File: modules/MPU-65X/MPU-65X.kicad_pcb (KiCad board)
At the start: 2 copper layers, 160 x 100 mm, 11 parts, among them J1 CardConnector, J2 DE9_Socket, U1 6502, U2 28C256, U3 62256, U4 74NC00, U5 W65C51, U6 W65C22, U8 MAX232, Y1 1Mhz

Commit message: added joshua
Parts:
- added D1: RI, LED_THT:LED_D5.0mm_Horizontal_O1.27mm_Z9.0mm, F.Cu at (65.2, 56.9)
- added D2: DTR, LED_THT:LED_D5.0mm_Horizontal_O1.27mm_Z9.0mm, F.Cu at (65.2, 63.5)
- added D3: DCD, LED_THT:LED_D5.0mm_Horizontal_O1.27mm_Z9.0mm, F.Cu at (65.2, 70.1)
- added D4: DSR, LED_THT:LED_D5.0mm_Horizontal_O1.27mm_Z9.0mm, F.Cu at (65.2, 76.7)
- added D5: RTS, LED_THT:LED_D5.0mm_Horizontal_O1.27mm_Z3.0mm, F.Cu at (62.0, 70.1)
- added D6: RTR, LED_THT:LED_D5.0mm_Horizontal_O1.27mm_Z3.0mm, F.Cu at (62.0, 83.3)
- added D7: CTS, LED_THT:LED_D5.0mm_Horizontal_O1.27mm_Z3.0mm, F.Cu at (62.0, 76.7)
- added D8: T_{X}D, LED_THT:LED_D5.0mm_Horizontal_O1.27mm_Z3.0mm, F.Cu at (62.0, 56.9)
- added D9: R_{X}D, LED_THT:LED_D5.0mm_Horizontal_O1.27mm_Z3.0mm, F.Cu at (62.0, 63.5)
- added R1: 1kΩ, IMNOTWOPR:R_Axial_DIN0207_P400mil, F.Cu at (74.7, 59.4)
- added R2: 1kΩ, IMNOTWOPR:R_Axial_DIN0207_P400mil, F.Cu at (74.7, 63.3)
- added R3: 1kΩ, IMNOTWOPR:R_Axial_DIN0207_P400mil, F.Cu at (74.7, 67.2)
- added R4: 1kΩ, IMNOTWOPR:R_Axial_DIN0207_P400mil, F.Cu at (74.7, 71.0)
- added R5: 1kΩ, IMNOTWOPR:R_Axial_DIN0207_P400mil, F.Cu at (74.7, 74.9)
- added R6: 1kΩ, IMNOTWOPR:R_Axial_DIN0207_P400mil, F.Cu at (74.7, 78.7)
- added R7: 1kΩ, IMNOTWOPR:R_Axial_DIN0207_P400mil, F.Cu at (74.7, 82.6)
- added R8: 1kΩ, IMNOTWOPR:R_Axial_DIN0207_P400mil, F.Cu at (74.7, 86.5)
- added R9: 1kΩ, IMNOTWOPR:R_Axial_DIN0207_P400mil, F.Cu at (74.7, 90.3)
- moved U2 15.7 mm to (105.5, 74.0)
- moved U4 2.39 mm to (154.1, 72.2)
- moved J2 2.28 mm to (68.3, 124.2)

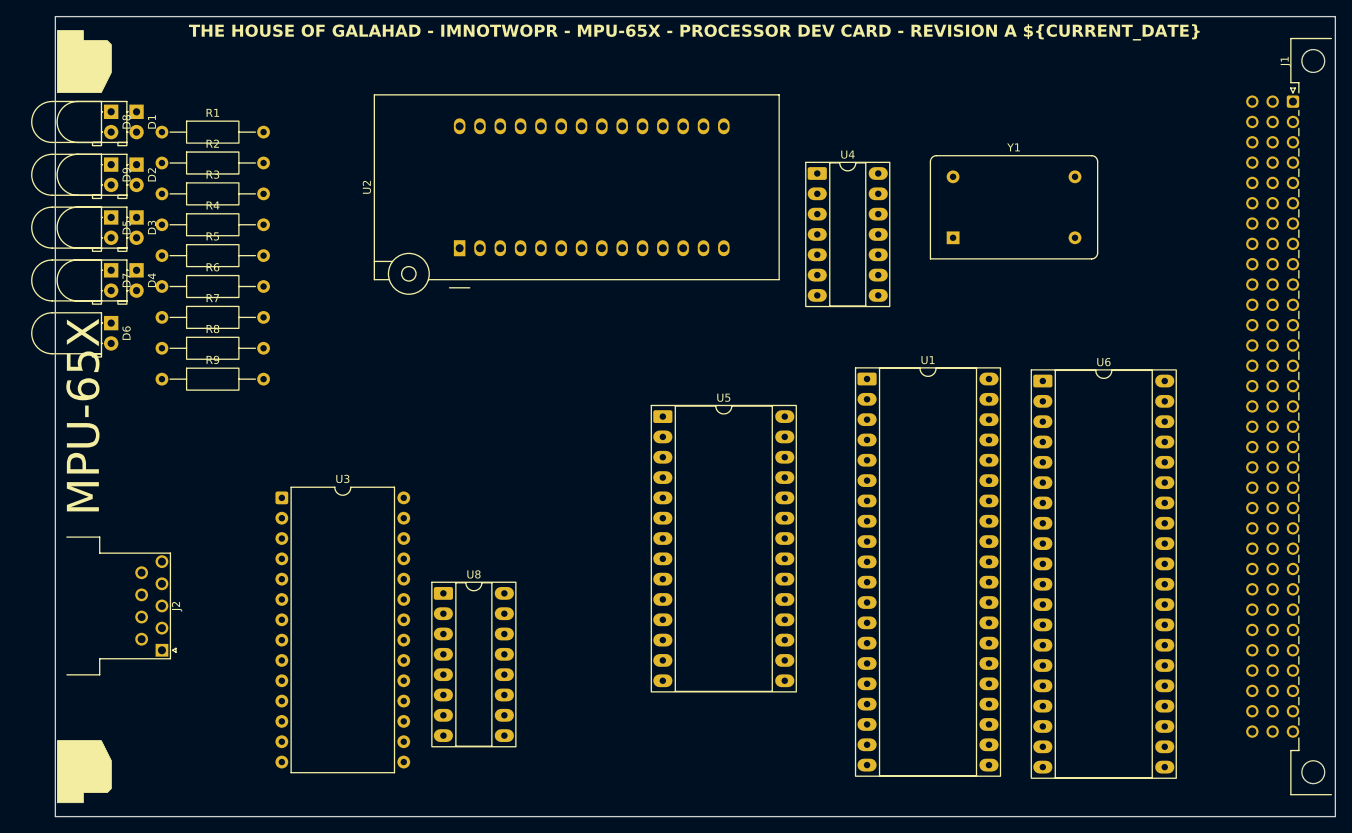
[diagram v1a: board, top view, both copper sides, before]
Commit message: mpu-65x circuit & pcb
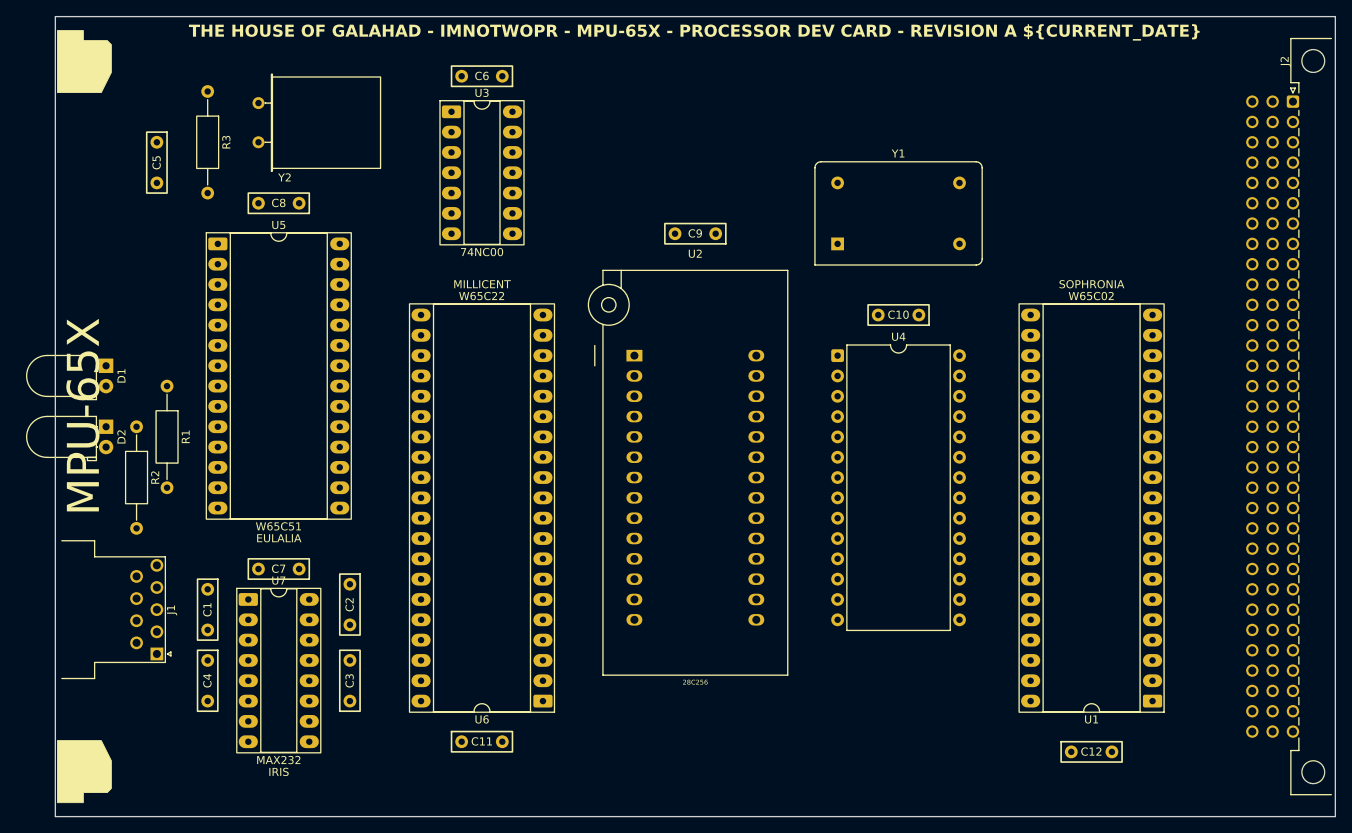
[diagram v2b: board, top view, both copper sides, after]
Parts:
- removed the D1 at (65.2, 56.9)
- removed the D2 at (65.2, 63.5)
- removed D3: DCD, LED_THT:LED_D5.0mm_Horizontal_O1.27mm_Z9.0mm
- removed D4: DSR, LED_THT:LED_D5.0mm_Horizontal_O1.27mm_Z9.0mm
- removed D5: RTS, LED_THT:LED_D5.0mm_Horizontal_O1.27mm_Z3.0mm
- removed D6: RTR, LED_THT:LED_D5.0mm_Horizontal_O1.27mm_Z3.0mm
- removed D7: CTS, LED_THT:LED_D5.0mm_Horizontal_O1.27mm_Z3.0mm
- removed the R1 at (74.7, 59.4)
- removed the R2 at (74.7, 63.3)
- removed R4, R5, R6, R7: 1kΩ, IMNOTWOPR:R_Axial_DIN0207_P400mil
- added C1: 1µF, IMNOTWOPR:C_Rect_P200mil, F.Cu at (74.0, 119.1)
- added C10: 100nF, IMNOTWOPR:C_Rect_P200mil, F.Cu at (160.4, 82.3)
- added C11: 100nF, IMNOTWOPR:C_Rect_P200mil, F.Cu at (108.3, 135.6)
- added C12: 100nF, IMNOTWOPR:C_Rect_P200mil, F.Cu at (184.5, 136.9)
- added C2: 1µF, IMNOTWOPR:C_Rect_P200mil, F.Cu at (91.8, 118.5)
- added C3: 1µF, IMNOTWOPR:C_Rect_P200mil, F.Cu at (91.8, 128.0)
- added C4: 1µF, IMNOTWOPR:C_Rect_P200mil, F.Cu at (74.0, 128.0)
- added C5: 20pF, IMNOTWOPR:C_Rect_P200mil, F.Cu at (67.7, 63.2)
- added C6: 100nF, IMNOTWOPR:C_Rect_P200mil, F.Cu at (108.3, 52.5)
- added C7: 100nF, IMNOTWOPR:C_Rect_P200mil, F.Cu at (82.9, 114.0)
- added C8: 100nF, IMNOTWOPR:C_Rect_P200mil, F.Cu at (82.9, 68.3)
- added C9: 100nF, IMNOTWOPR:C_Rect_P200mil, F.Cu at (135.0, 72.1)
- added Y2: Crystal, Crystal:Crystal_HC49-U_Horizontal, F.Cu at (80.4, 60.7)
- R3: value 1kΩ -> 1MΩ
- U1: value 6502 -> W65C02
- U2: footprint Socket:DIP_Socket-28_W11.9mm_W12.7mm_W15.24mm_W17.78mm_W18.5mm_3M_228-1277-00-0602J -> IMNOTWOPR:ZIF-28W
- moved U6 78.2 mm to (108.3, 106.4), turned to 180 degrees
- moved U4 71.7 mm to (152.8, 87.4)
- moved U5 59.7 mm to (82.9, 89.9)
- moved U3 46.4 mm to (108.3, 64.5)
- moved D2 32.8 mm to (61.3, 96.3)
- moved D1 31.8 mm to (61.3, 88.7)
- moved U2 25.6 mm to (127.4, 87.4), turned to 0 degrees
- moved U7 24.4 mm to (82.9, 126.8)
- moved U1 22.0 mm to (184.5, 106.4), turned to 180 degrees
- moved R2 15.6 mm to (65.2, 102.6), turned to -90 degrees
- moved Y1 14.5 mm to (152.8, 73.4)
- moved R1 12.5 mm to (69.0, 97.5), turned to -90 degrees
- moved R3 6.48 mm to (74.0, 60.7), turned to -90 degrees
- moved J1 0.78 mm to (67.7, 124.7)
- renumbered D8 to D1, D9 to D2, J2 to J1, J1 to J2, R8 to R1, R9 to R2, U4 to U3, U3 to U4, U8 to U7
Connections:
- J1 pad 2: unconnected-(J2-Pad2) -> T_{X}D
- J1 pad 3: unconnected-(J2-Pad3) -> R_{X}D
- J1 pad 5: unconnected-(J2-Pad5) -> GND
- R3 pad 2: RTR -> Net-(R3-Pad2)
- U1 pad 10: unconnected-(U1-A_{1}-Pad10) -> /MPU-65X/A_{1}
- U1 pad 11: unconnected-(U1-A_{2}-Pad11) -> /MPU-65X/A_{2}
- U1 pad 12: unconnected-(U1-A_{3}-Pad12) -> /MPU-65X/A_{3}
- U1 pad 13: unconnected-(U1-A_{4}-Pad13) -> /MPU-65X/A_{4}
- U1 pad 14: unconnected-(U1-A_{5}-Pad14) -> /MPU-65X/A_{5}
- U1 pad 15: unconnected-(U1-A_{6}-Pad15) -> /MPU-65X/A_{6}
- U1 pad 16: unconnected-(U1-A_{7}-Pad16) -> /MPU-65X/A_{7}
- U1 pad 17: unconnected-(U1-A_{8}-Pad17) -> /MPU-65X/A_{8}
- U1 pad 18: unconnected-(U1-A_{9}-Pad18) -> /MPU-65X/A_{9}
- U1 pad 19: unconnected-(U1-A_{10}-Pad19) -> /MPU-65X/A_{10}
- U1 pad 20: unconnected-(U1-A_{11}-Pad20) -> /MPU-65X/A_{11}
- U1 pad 22: unconnected-(U1-A_{12}-Pad22) -> /MPU-65X/A_{12}
- U1 pad 23: unconnected-(U1-A_{13}-Pad23) -> /MPU-65X/A_{13}
- U1 pad 24: unconnected-(U1-A_{14}-Pad24) -> /MPU-65X/A_{14}
- U1 pad 26: unconnected-(U1-D_{7}-Pad26) -> /MPU-65X/D_{7}
- U1 pad 27: unconnected-(U1-D_{6}-Pad27) -> /MPU-65X/D_{6}
- U1 pad 28: unconnected-(U1-D_{5}-Pad28) -> /MPU-65X/D_{5}
- U1 pad 29: unconnected-(U1-D_{4}-Pad29) -> /MPU-65X/D_{4}
- U1 pad 30: unconnected-(U1-D_{3}-Pad30) -> /MPU-65X/D_{3}
- U1 pad 31: unconnected-(U1-D_{2}-Pad31) -> /MPU-65X/D_{2}
- U1 pad 32: unconnected-(U1-D_{1}-Pad32) -> /MPU-65X/D_{1}
- U1 pad 33: unconnected-(U1-D_{0}-Pad33) -> /MPU-65X/D_{0}
- U1 pad 9: unconnected-(U1-A_{0}-Pad9) -> /MPU-65X/A_{0}
- U2 pad 1: unconnected-(U2-A14-Pad1) -> /MPU-65X/A_{14}
- U2 pad 10: unconnected-(U2-A0-Pad10) -> /MPU-65X/A_{0}
- U2 pad 11: unconnected-(U2-D0-Pad11) -> /MPU-65X/D_{0}
- U2 pad 12: unconnected-(U2-D1-Pad12) -> /MPU-65X/D_{1}
- U2 pad 13: unconnected-(U2-D2-Pad13) -> /MPU-65X/D_{2}
- U2 pad 15: unconnected-(U2-D3-Pad15) -> /MPU-65X/D_{3}
- U2 pad 16: unconnected-(U2-D4-Pad16) -> /MPU-65X/D_{4}
- U2 pad 17: unconnected-(U2-D5-Pad17) -> /MPU-65X/D_{5}
- U2 pad 18: unconnected-(U2-D6-Pad18) -> /MPU-65X/D_{6}
- U2 pad 19: unconnected-(U2-D7-Pad19) -> /MPU-65X/D_{7}
- U2 pad 2: unconnected-(U2-A12-Pad2) -> /MPU-65X/A_{12}
- U2 pad 20: unconnected-(U2-~{CS}-Pad20) -> Net-(U2-~{CS})
- U2 pad 21: unconnected-(U2-A10-Pad21) -> /MPU-65X/A_{10}
- U2 pad 22: unconnected-(U2-~{OE}-Pad22) -> GND
- U2 pad 23: unconnected-(U2-A11-Pad23) -> /MPU-65X/A_{11}
- U2 pad 24: unconnected-(U2-A9-Pad24) -> /MPU-65X/A_{9}
- U2 pad 25: unconnected-(U2-A8-Pad25) -> /MPU-65X/A_{8}
- U2 pad 26: unconnected-(U2-A13-Pad26) -> /MPU-65X/A_{13}
- U2 pad 27: unconnected-(U2-~{WE}-Pad27) -> VCC
- U2 pad 3: unconnected-(U2-A7-Pad3) -> /MPU-65X/A_{7}
- U2 pad 4: unconnected-(U2-A6-Pad4) -> /MPU-65X/A_{6}
- U2 pad 5: unconnected-(U2-A5-Pad5) -> /MPU-65X/A_{5}
- U2 pad 6: unconnected-(U2-A4-Pad6) -> /MPU-65X/A_{4}
- U2 pad 7: unconnected-(U2-A3-Pad7) -> /MPU-65X/A_{3}
- U2 pad 8: unconnected-(U2-A2-Pad8) -> /MPU-65X/A_{2}
- U2 pad 9: unconnected-(U2-A1-Pad9) -> /MPU-65X/A_{1}
- U3 pad 1: unconnected-(U4-Pad1) -> GND
- U3 pad 10: unconnected-(U4-Pad10) -> Net-(U2-~{CS})
- U3 pad 11: unconnected-(U4-Pad11) -> Net-(U2-~{CS})
- U3 pad 12: unconnected-(U4-Pad12) -> /MPU-65X/A_{15}
- U3 pad 13: unconnected-(U4-Pad13) -> /MPU-65X/A_{15}
- U3 pad 14: unconnected-(U4E-VCC-Pad14) -> VCC
- U3 pad 2: unconnected-(U4-Pad2) -> GND
- U3 pad 4: unconnected-(U4-Pad4) -> /MPU-65X/A_{14}
- U3 pad 5: unconnected-(U4-Pad5) -> Net-(U2-~{CS})
- U3 pad 7: unconnected-(U4E-GND-Pad7) -> GND
- U3 pad 8: unconnected-(U4-Pad8) -> Net-(U4-~{CS})
- U4 pad 1: unconnected-(U3-A14-Pad1) -> /MPU-65X/A_{14}
- U4 pad 10: unconnected-(U3-A0-Pad10) -> /MPU-65X/A_{0}
- U4 pad 11: unconnected-(U3-Q0-Pad11) -> /MPU-65X/D_{0}
- U4 pad 12: unconnected-(U3-Q1-Pad12) -> /MPU-65X/D_{1}
- U4 pad 13: unconnected-(U3-Q2-Pad13) -> /MPU-65X/D_{2}
- U4 pad 15: unconnected-(U3-Q3-Pad15) -> /MPU-65X/D_{3}
- U4 pad 16: unconnected-(U3-Q4-Pad16) -> /MPU-65X/D_{4}
- U4 pad 17: unconnected-(U3-Q5-Pad17) -> /MPU-65X/D_{5}
- U4 pad 18: unconnected-(U3-Q6-Pad18) -> /MPU-65X/D_{6}
- U4 pad 19: unconnected-(U3-Q7-Pad19) -> /MPU-65X/D_{7}
- U4 pad 2: unconnected-(U3-A12-Pad2) -> /MPU-65X/A_{12}
- U4 pad 20: unconnected-(U3-~{CS}-Pad20) -> Net-(U4-~{CS})
- U4 pad 21: unconnected-(U3-A10-Pad21) -> /MPU-65X/A_{10}
- U4 pad 22: unconnected-(U3-~{OE}-Pad22) -> /MPU-65X/A_{14}
- U4 pad 23: unconnected-(U3-A11-Pad23) -> /MPU-65X/A_{11}
- U4 pad 24: unconnected-(U3-A9-Pad24) -> /MPU-65X/A_{9}
- U4 pad 25: unconnected-(U3-A8-Pad25) -> /MPU-65X/A_{8}
- U4 pad 26: unconnected-(U3-A13-Pad26) -> /MPU-65X/A_{13}
- U4 pad 3: unconnected-(U3-A7-Pad3) -> /MPU-65X/A_{7}
- U4 pad 4: unconnected-(U3-A6-Pad4) -> /MPU-65X/A_{6}
- U4 pad 5: unconnected-(U3-A5-Pad5) -> /MPU-65X/A_{5}
- U4 pad 6: unconnected-(U3-A4-Pad6) -> /MPU-65X/A_{4}
- U4 pad 7: unconnected-(U3-A3-Pad7) -> /MPU-65X/A_{3}
- U4 pad 8: unconnected-(U3-A2-Pad8) -> /MPU-65X/A_{2}
- U4 pad 9: unconnected-(U3-A1-Pad9) -> /MPU-65X/A_{1}
- U5 pad 1: unconnected-(U5-V_{SS}-Pad1) -> GND
- U5 pad 10: unconnected-(U5-TX_{D}-Pad10) -> Net-(U5-TX_{D})
- U5 pad 12: unconnected-(U5-R_{X}D-Pad12) -> Net-(U5-R_{X}D)
- U5 pad 15: unconnected-(U5-V_{DD}-Pad15) -> VCC
- U5 pad 18: unconnected-(U5-D_{0}-Pad18) -> /MPU-65X/D_{0}
- U5 pad 19: unconnected-(U5-D_{1}-Pad19) -> /MPU-65X/D_{1}
- U5 pad 20: unconnected-(U5-D_{2}-Pad20) -> /MPU-65X/D_{2}
- U5 pad 21: unconnected-(U5-D_{3}-Pad21) -> /MPU-65X/D_{3}
- U5 pad 22: unconnected-(U5-D_{4}-Pad22) -> /MPU-65X/D_{4}
- U5 pad 23: unconnected-(U5-D_{5}-Pad23) -> /MPU-65X/D_{5}
- U5 pad 24: unconnected-(U5-D_{6}-Pad24) -> /MPU-65X/D_{6}
- U5 pad 25: unconnected-(U5-D_{7}-Pad25) -> /MPU-65X/D_{7}
- U6 pad 1: unconnected-(U6-V_{SS}-Pad1) -> GND
- U6 pad 20: unconnected-(U6-V_{DD}-Pad20) -> VCC
- U6 pad 26: unconnected-(U6-D_{7}-Pad26) -> /MPU-65X/D_{7}
- U6 pad 27: unconnected-(U6-D_{6}-Pad27) -> /MPU-65X/D_{6}
- U6 pad 28: unconnected-(U6-D_{5}-Pad28) -> /MPU-65X/D_{5}
- U6 pad 29: unconnected-(U6-D_{4}-Pad29) -> /MPU-65X/D_{4}
- U6 pad 30: unconnected-(U6-D_{3}-Pad30) -> /MPU-65X/D_{3}
- U6 pad 31: unconnected-(U6-D_{2}-Pad31) -> /MPU-65X/D_{2}
- U6 pad 32: unconnected-(U6-D_{1}-Pad32) -> /MPU-65X/D_{1}
- U6 pad 33: unconnected-(U6-D_{0}-Pad33) -> /MPU-65X/D_{0}
- U7 pad 1: unconnected-(U8-C1+-Pad1) -> Net-(U7-C1+)
- U7 pad 11: unconnected-(U8-T1IN-Pad11) -> Net-(U5-TX_{D})
- U7 pad 12: unconnected-(U8-R1OUT-Pad12) -> Net-(U5-R_{X}D)
- U7 pad 13: unconnected-(U8-R1IN-Pad13) -> R_{X}D
- U7 pad 14: unconnected-(U8-T1OUT-Pad14) -> T_{X}D
- U7 pad 15: unconnected-(U8-GND-Pad15) -> GND
- U7 pad 16: unconnected-(U8-VCC-Pad16) -> VCC
- U7 pad 2: unconnected-(U8-VS+-Pad2) -> Net-(U7-VS+)
- U7 pad 3: unconnected-(U8-C1--Pad3) -> Net-(U7-C1-)
- U7 pad 4: unconnected-(U8-C2+-Pad4) -> Net-(U7-C2+)
- U7 pad 5: unconnected-(U8-C2--Pad5) -> Net-(U7-C2-)
- U7 pad 6: unconnected-(U8-VS--Pad6) -> Net-(U7-VS-)

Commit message: Formatting and MPU-65X work
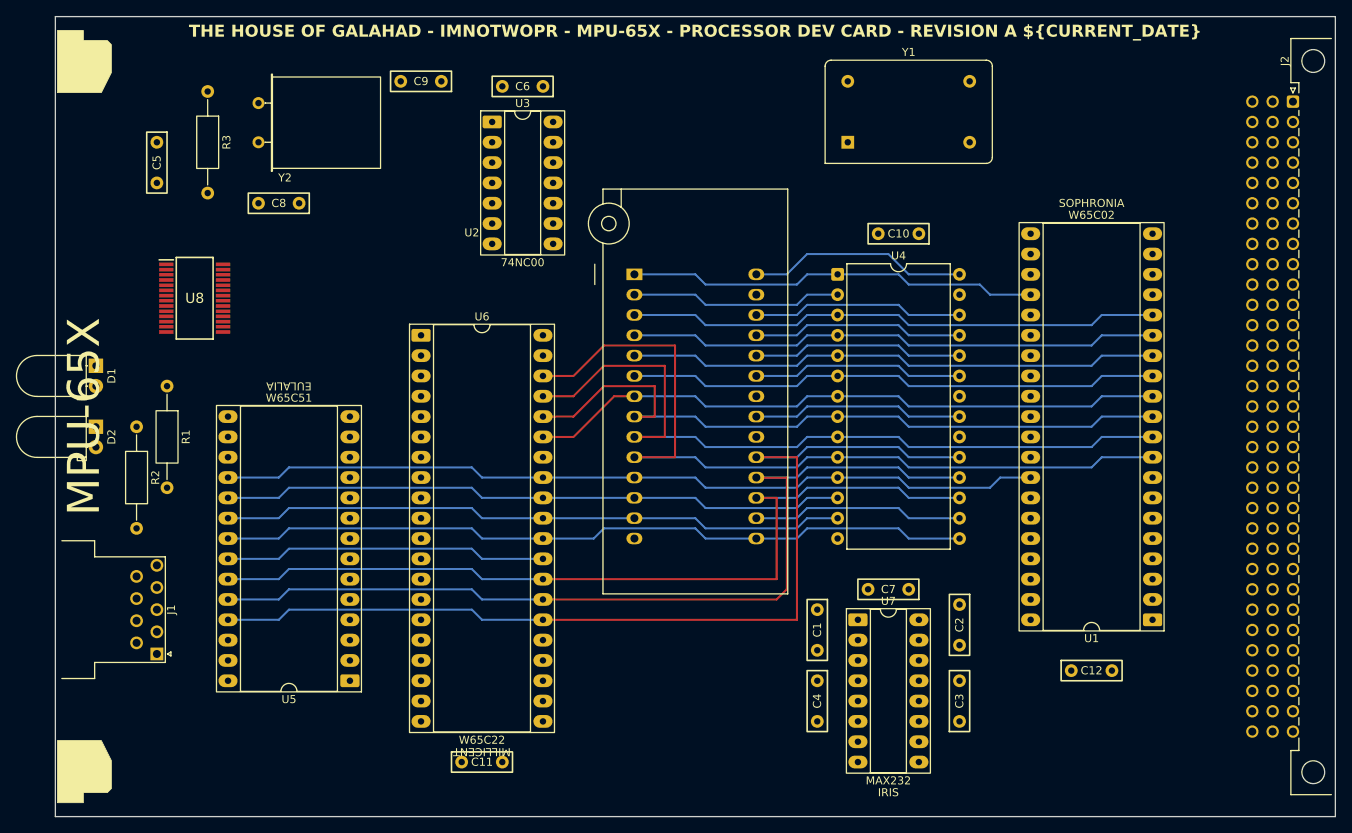
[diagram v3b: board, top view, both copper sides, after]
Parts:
- added U8: MAX3243IDBR, IMNOTWOPR:SOP65P780X200-28N, F.Cu at (72.4, 80.2)
- moved C2 76.2 mm to (168.0, 121.0)
- moved C3 76.2 mm to (168.0, 130.6)
- moved C1 76.2 mm to (150.2, 121.7)
- moved C4 76.2 mm to (150.2, 130.6)
- moved C7 76.2 mm to (159.1, 116.6)
- moved U7 76.2 mm to (159.1, 129.3)
- moved C9 39.2 mm to (100.7, 53.1)
- moved U5 21.6 mm to (84.2, 111.5), turned to 180 degrees
- moved Y1 12.8 mm to (154.1, 60.7)
- moved U1 10.2 mm to (184.5, 96.3)
- moved C10 10.2 mm to (160.4, 72.1)
- moved C12 10.2 mm to (184.5, 126.8)
- moved U2 10.2 mm to (127.4, 77.2)
- moved U4 10.2 mm to (152.8, 77.2)
- moved U3 5.24 mm to (113.4, 65.8)
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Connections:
- C5 pad 1: Net-(C5-Pad1) -> Net-(U5-XTLI)
- J2 pad b15: unconnected-(J2B-~{RESET}-Padb15) -> ~{RESET}
- R3 pad 1: Net-(C5-Pad1) -> Net-(U5-XTLI)
- R3 pad 2: Net-(R3-Pad2) -> Net-(U5-XTLO)
- U1 pad 40: unconnected-(U1-~{RES}-Pad40) -> ~{RESET}
- U3 pad 6: unconnected-(U3-Pad6) -> Net-(U6-~{CS_{2}})
- U5 pad 13: unconnected-(U5-RS_{0}-Pad13) -> /MPU-65X/A_{0}
- U5 pad 14: unconnected-(U5-RS_{1}-Pad14) -> /MPU-65X/A_{1}
- U5 pad 2: unconnected-(U5-CS_{0}-Pad2) -> /MPU-65X/A_{12}
- U5 pad 4: unconnected-(U5-~{RES}-Pad4) -> ~{RESET}
- U5 pad 6: unconnected-(U5-XTLI-Pad6) -> Net-(U5-XTLI)
- U5 pad 7: unconnected-(U5-XTLO-Pad7) -> Net-(U5-XTLO)
- U6 pad 23: unconnected-(U6-~{CS_{2}}-Pad23) -> Net-(U6-~{CS_{2}})
- U6 pad 24: unconnected-(U6-CS_{1}-Pad24) -> /MPU-65X/A_{13}
- U6 pad 34: unconnected-(U6-~{RES}-Pad34) -> ~{RESET}
- U6 pad 35: unconnected-(U6-RS_{3}-Pad35) -> /MPU-65X/A_{3}
- U6 pad 36: unconnected-(U6-RS_{2}-Pad36) -> /MPU-65X/A_{2}
- U6 pad 37: unconnected-(U6-RS_{1}-Pad37) -> /MPU-65X/A_{1}
- U6 pad 38: unconnected-(U6-RS_{0}-Pad38) -> /MPU-65X/A_{0}
- Y2 pad 1: Net-(R3-Pad2) -> Net-(U5-XTLO)
- Y2 pad 2: Net-(C5-Pad1) -> Net-(U5-XTLI)
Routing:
- net /MPU-65X/D_{7}: track 0.00 -> 124.0 mm
- net /MPU-65X/D_{6}: track 0.00 -> 115.7 mm
- net /MPU-65X/D_{5}: track 0.00 -> 108.8 mm
- net /MPU-65X/A_{0}: track 0.00 -> 104.0 mm
- net /MPU-65X/D_{0}: track 0.00 -> 103.5 mm
- net /MPU-65X/A_{1}: track 0.00 -> 96.4 mm
- net /MPU-65X/D_{3}: track 0.00 -> 94.6 mm
- net /MPU-65X/A_{2}: track 0.00 -> 88.8 mm
- net /MPU-65X/A_{3}: track 0.00 -> 80.4 mm
- net /MPU-65X/D_{1}: track 0.00 -> 78.3 mm
- net /MPU-65X/D_{2}: track 0.00 -> 78.3 mm
- net /MPU-65X/A_{5}: track 0.00 -> 66.9 mm
- net /MPU-65X/D_{4}: track 0.00 -> 66.9 mm
- net /MPU-65X/A_{6}: track 0.00 -> 66.9 mm
- net /MPU-65X/A_{7}: track 0.00 -> 66.9 mm
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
